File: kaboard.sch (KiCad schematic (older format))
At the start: 22 parts, among them IC1 ATMEGA8-P, K1 CONN_3, K2 CONN_3, K3 CONN_3, P1 CONN_6, P2 CONN_6, P3 CONN_6, P4 CONN_6, P5 CONN_5, P6 CONN_6, P7 CONN_5, P8 CONN_6, P9 CONN_5, SW1 SW_PUSH, X1 CRYSTAL

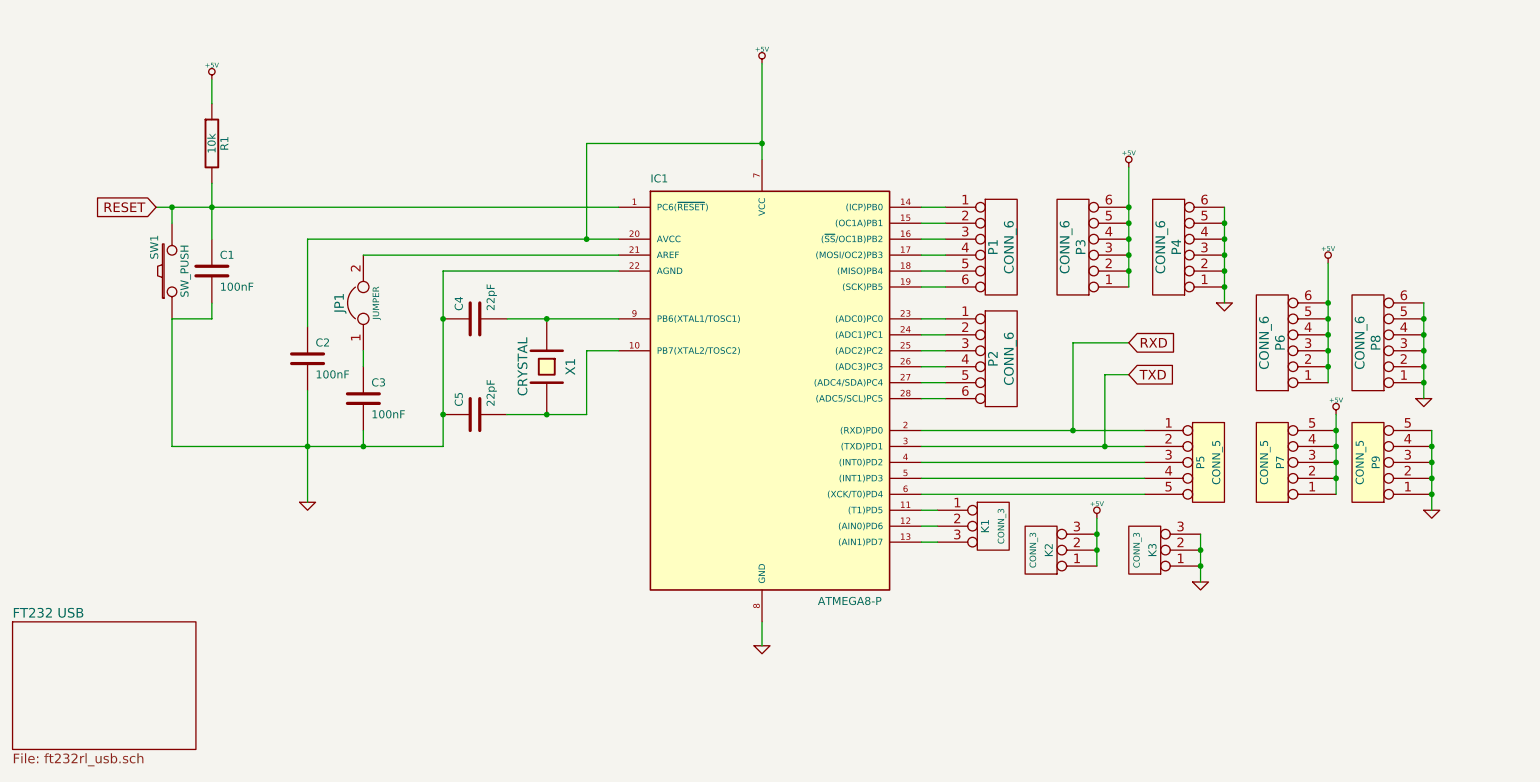
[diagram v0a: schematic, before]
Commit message: - Second version of the board - Added README for github
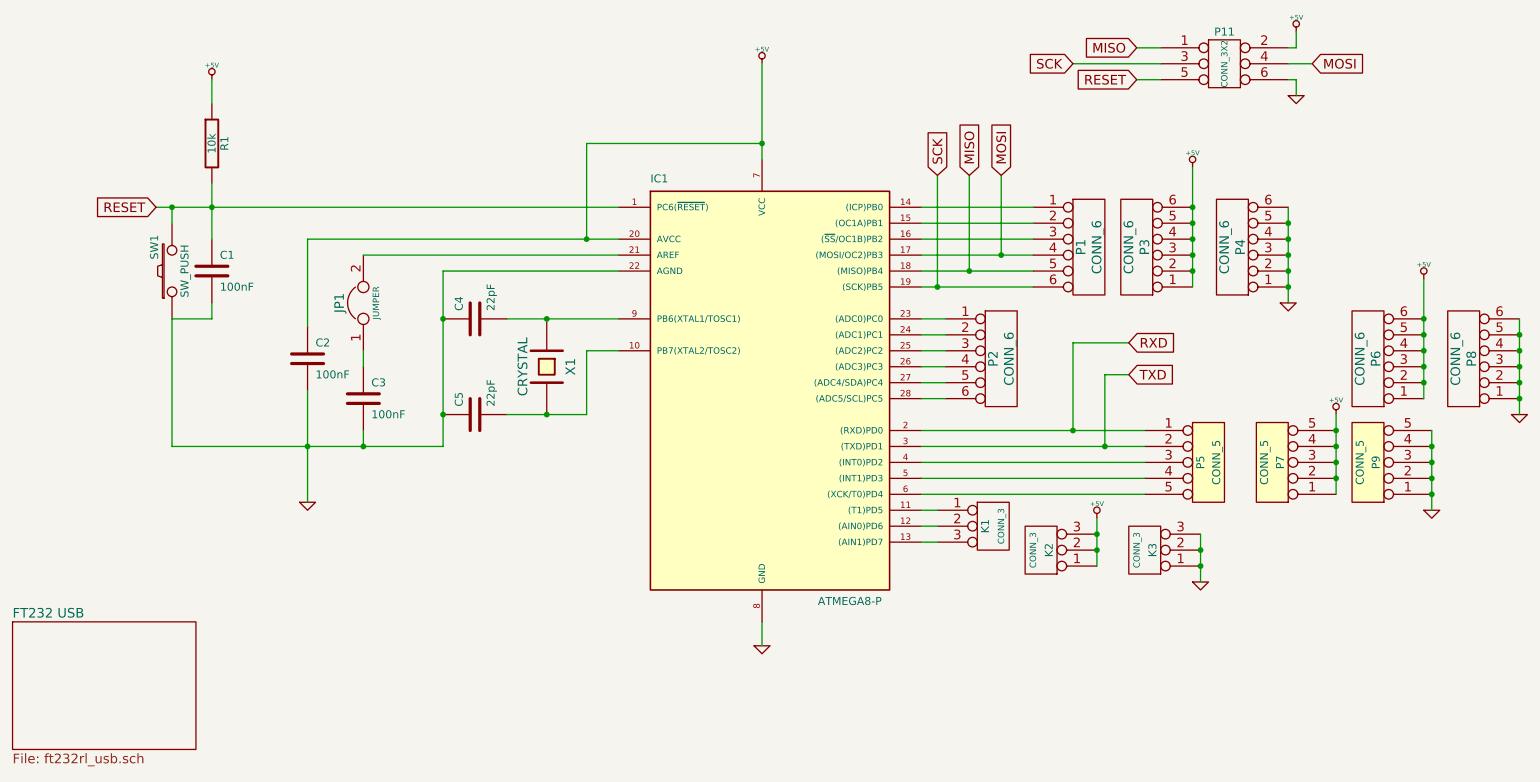
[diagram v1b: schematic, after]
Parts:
- added P11: CONN_3X2, symbol CONN_3X2
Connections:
- net +5V: now also P11.2
- net GND: now also P11.6
- net RESET: now also P11.5
- net MOSI: now reaches IC1.17 ((MOSI/OC2)PB3), P1.4
- net MOSI: now also P11.4
- net MISO: now reaches IC1.18 ((MISO)PB4), P1.5
- net MISO: now also P11.1
- net SCK: now reaches IC1.19 ((SCK)PB5), P1.6
- net SCK: now also P11.3
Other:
- moved on the sheet: P1, P3, P4, P6, P8
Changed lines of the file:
@@
-EESchema Schematic File Version 2  date Sun 09 Dec 2012 11:53:08 PM CET
+EESchema Schematic File Version 2  date Thu 13 Dec 2012 04:01:05 PM CET
 LIBS:power
 LIBS:device
@@
 Sheet 1 2
 Title ""
-Date "9 dec 2012"
+Date "13 dec 2012"
 Rev ""
 Comp ""
@@
 Connection ~ 9750 5450
 Wire Wire Line
-	9750 5550 9750 5050
+	9750 5050 9750 5550
 Connection ~ 9750 5250
 Connection ~ 9150 5250
 Connection ~ 9150 5050
-Connection ~ 9700 4350
+Connection ~ 10300 4450
+Connection ~ 10300 4650
 Connection ~ 9700 4550
-Connection ~ 9100 4450
-Connection ~ 9100 4650
-Connection ~ 9100 4550
-Connection ~ 9100 4350
+Connection ~ 9700 4750
 Connection ~ 9700 4650
 Connection ~ 9700 4450
-Wire Wire Line
-	9100 4000 9100 4750
-Connection ~ 9100 4250
-Wire Wire Line
-	9700 4850 9700 4250
-Connection ~ 9700 4750
-Connection ~ 8450 4150
-Wire Wire Line
-	8450 4250 8450 3650
-Connection ~ 7850 3650
-Wire Wire Line
-	7850 3400 7850 4150
-Connection ~ 8450 3850
-Connection ~ 8450 4050
-Connection ~ 7850 3750
-Connection ~ 7850 3950
+Connection ~ 10300 4750
+Connection ~ 10300 4550
+Wire Wire Line
+	9700 4100 9700 4850
+Connection ~ 9700 4350
+Wire Wire Line
+	10300 4350 10300 4950
+Connection ~ 10300 4850
+Connection ~ 8850 4150
+Wire Wire Line
+	8850 3650 8850 4250
+Connection ~ 8250 3650
+Wire Wire Line
+	8250 3400 8250 4150
+Connection ~ 8850 3850
+Connection ~ 8850 4050
+Connection ~ 8250 3750
+Connection ~ 8250 3950
 Wire Wire Line
 	6550 5350 7950 5350
@@
 	6550 5550 6650 5550
 Wire Wire Line
-	7950 5150 6550 5150
+	6550 5150 7950 5150
 Wire Wire Line
 	6550 4850 6700 4850
@@
 	6550 4450 6700 4450
 Wire Wire Line
-	6550 4150 6700 4150
-Wire Wire Line
-	6550 3950 6700 3950
-Wire Wire Line
-	6550 3750 6700 3750
+	6550 4150 7250 4150
+Wire Wire Line
+	6550 3950 7250 3950
+Wire Wire Line
+	6550 3750 7250 3750
 Wire Wire Line
 	5550 6400 5550 6250
@@
 Connection ~ 3550 4350
 Wire Wire Line
-	4650 3850 2700 3850
-Wire Wire Line
-	4650 4350 3950 4350
+	2700 3850 4650 3850
+Wire Wire Line
+	3950 4350 4650 4350
 Connection ~ 4200 4950
 Wire Wire Line
@@
 	4450 3250 5550 3250
 Wire Wire Line
-	2100 3850 2100 3500
+	2100 3500 2100 3850
 Wire Wire Line
 	5550 2750 5550 3350
@@
 Connection ~ 3050 5150
 Wire Wire Line
-	2700 5500 2700 4800
-Wire Wire Line
-	6550 3650 6700 3650
-Wire Wire Line
-	6550 3850 6700 3850
-Wire Wire Line
-	6550 4050 6700 4050
+	2700 4800 2700 5500
+Wire Wire Line
+	6550 3650 7250 3650
+Wire Wire Line
+	6550 3850 7250 3850
+Wire Wire Line
+	6550 4050 7250 4050
 Wire Wire Line
 	6700 4350 6550 4350
@@
 	6550 4750 6700 4750
 Wire Wire Line
-	7950 5050 6550 5050
+	6550 5050 7950 5050
 Wire Wire Line
 	7950 5250 6550 5250
@@
 Wire Wire Line
 	6550 5450 7950 5450
-Connection ~ 7850 4050
-Connection ~ 7850 3850
-Connection ~ 8450 3950
-Connection ~ 8450 3750
+Connection ~ 8250 4050
+Connection ~ 8250 3850
+Connection ~ 8850 3950
+Connection ~ 8850 3750
 Connection ~ 9150 5150
 Wire Wire Line
-	9150 5450 9150 4950
+	9150 4950 9150 5450
 Connection ~ 9150 5350
 Connection ~ 9750 5150
 Connection ~ 9750 5350
 Wire Wire Line
-	8300 6000 8300 5700
+	8300 5700 8300 6000
 Connection ~ 8300 5900
 Text GLabel 1750 3650 0    60   Input ~ 0
@@
 L CONN_6 P6
 U 1 1 5069D2A4
-P 8750 4500
-F 0 "P6" V 8700 4500 60  0000 C CNN
-F 1 "CONN_6" V 8800 4500 60  0000 C CNN
-	1    8750 4500
+P 9350 4600
+F 0 "P6" V 9300 4600 60  0000 C CNN
+F 1 "CONN_6" V 9400 4600 60  0000 C CNN
+	1    9350 4600
 	-1   0    0    1
 $EndComp
@@
 L CONN_6 P8
 U 1 1 5069D2A3
-P 9350 4500
-F 0 "P8" V 9300 4500 60  0000 C CNN
-F 1 "CONN_6" V 9400 4500 60  0000 C CNN
-	1    9350 4500
+P 9950 4600
+F 0 "P8" V 9900 4600 60  0000 C CNN
+F 1 "CONN_6" V 10000 4600 60  0000 C CNN
+	1    9950 4600
 	-1   0    0    1
 $EndComp
@@
 L GND #PWR06
 U 1 1 5069D2A2
-P 9700 4850
-F 0 "#PWR06" H 9700 4850 30  0001 C CNN
-F 1 "GND" H 9700 4780 30  0001 C CNN
-	1    9700 4850
+P 10300 4950
+F 0 "#PWR06" H 10300 4950 30  0001 C CNN
+F 1 "GND" H 10300 4880 30  0001 C CNN
+	1    10300 4950
 	1    0    0    -1
 $EndComp
@@
 L +5V #PWR07
 U 1 1 5069D2A1
-P 9100 4000
-F 0 "#PWR07" H 9100 4090 20  0001 C CNN
-F 1 "+5V" H 9100 4090 30  0000 C CNN
-	1    9100 4000
+P 9700 4100
+F 0 "#PWR07" H 9700 4190 20  0001 C CNN
+F 1 "+5V" H 9700 4190 30  0000 C CNN
+	1    9700 4100
 	1    0    0    -1
 $EndComp
@@
 L +5V #PWR08
 U 1 1 5069D26F
-P 7850 3400
-F 0 "#PWR08" H 7850 3490 20  0001 C CNN
-F 1 "+5V" H 7850 3490 30  0000 C CNN
-	1    7850 3400
+P 8250 3400
+F 0 "#PWR08" H 8250 3490 20  0001 C CNN
+F 1 "+5V" H 8250 3490 30  0000 C CNN
+	1    8250 3400
 	1    0    0    -1
 $EndComp
@@
 L GND #PWR09
 U 1 1 5069D267
-P 8450 4250
-F 0 "#PWR09" H 8450 4250 30  0001 C CNN
-F 1 "GND" H 8450 4180 30  0001 C CNN
-	1    8450 4250
+P 8850 4250
+F 0 "#PWR09" H 8850 4250 30  0001 C CNN
+F 1 "GND" H 8850 4180 30  0001 C CNN
+	1    8850 4250
 	1    0    0    -1
 $EndComp
@@
 L CONN_6 P4
 U 1 1 5069D139
-P 8100 3900
-F 0 "P4" V 8050 3900 60  0000 C CNN
-F 1 "CONN_6" V 8150 3900 60  0000 C CNN
-	1    8100 3900
+P 8500 3900
+F 0 "P4" V 8450 3900 60  0000 C CNN
+F 1 "CONN_6" V 8550 3900 60  0000 C CNN
+	1    8500 3900
 	-1   0    0    1
 $EndComp
@@
 L CONN_6 P3
 U 1 1 5069D130
-P 7500 3900
-F 0 "P3" V 7450 3900 60  0000 C CNN
-F 1 "CONN_6" V 7550 3900 60  0000 C CNN
-	1    7500 3900
+P 7900 3900
+F 0 "P3" V 7850 3900 60  0000 C CNN
+F 1 "CONN_6" V 7950 3900 60  0000 C CNN
+	1    7900 3900
 	-1   0    0    1
 $EndComp
@@
 L CONN_6 P1
 U 1 1 5069CE7E
-P 7050 3900
-F 0 "P1" V 7000 3900 60  0000 C CNN
-F 1 "CONN_6" V 7100 3900 60  0000 C CNN
-	1    7050 3900
+P 7600 3900
+F 0 "P1" V 7550 3900 60  0000 C CNN
+F 1 "CONN_6" V 7650 3900 60  0000 C CNN
+	1    7600 3900
 	1    0    0    -1
 $EndComp
@@
 F1 "ft232rl_usb.sch" 60
 $EndSheet
+$Comp
+L CONN_3X2 P11
+U 1 1 50C6F989
+P 8450 2800
+F 0 "P11" H 8450 3050 50  0000 C CNN
+F 1 "CONN_3X2" V 8450 2850 40  0000 C CNN
+	1    8450 2800
+	1    0    0    -1
+$EndComp
+$Comp
+L GND #PWR013
+U 1 1 50C6F9DA
+P 8900 2950
+F 0 "#PWR013" H 8900 2950 30  0001 C CNN
+F 1 "GND" H 8900 2880 30  0001 C CNN
+	1    8900 2950
+	1    0    0    -1
+$EndComp
+Wire Wire Line
+	8900 2950 8900 2850
+Wire Wire Line
+	8900 2850 8850 2850
+$Comp
+L +5V #PWR014
+U 1 1 50C6FA7D
+P 8900 2550
+F 0 "#PWR014" H 8900 2640 20  0001 C CNN
+F 1 "+5V" H 8900 2640 30  0000 C CNN
+	1    8900 2550
+	1    0    0    -1
+$EndComp
+Wire Wire Line
+	8850 2650 8900 2650
+Wire Wire Line
+	8900 2650 8900 2550
+Text GLabel 7900 2850 0    60   Input ~ 0
+RESET
+Wire Wire Line
+	7900 2850 8050 2850
+Text GLabel 7500 2750 0    60   Input ~ 0
+SCK
+Text GLabel 7900 2650 0    60   Input ~ 0
+MISO
+Wire Wire Line
+	7900 2650 8050 2650
+Wire Wire Line
+	7500 2750 8050 2750
+Text GLabel 9000 2750 2    60   Input ~ 0
+MOSI
+Wire Wire Line
+	8850 2750 9000 2750
+Text GLabel 6650 3450 1    60   Input ~ 0
+SCK
+Wire Wire Line
+	6650 4150 6650 3450
+Connection ~ 6650 4150
+Text GLabel 6850 3450 1    60   Input ~ 0
+MISO
+Wire Wire Line
+	6850 4050 6850 3450
+Connection ~ 6850 4050
+Text GLabel 7050 3450 1    60   Input ~ 0
+MOSI
+Wire Wire Line
+	7050 3950 7050 3450
+Connection ~ 7050 3950
 $EndSCHEMATC

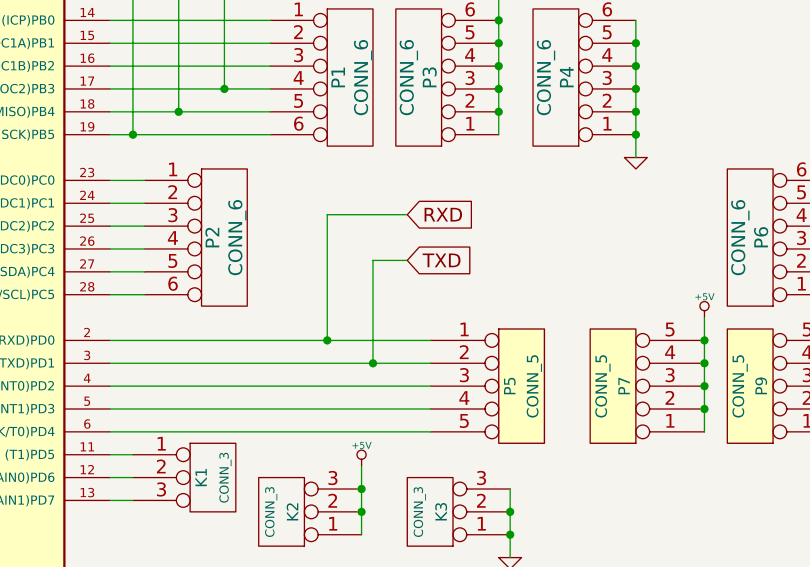
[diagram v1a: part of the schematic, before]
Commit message: Added list of known bugs on 1.0 Fixed the bugs and incremented version to 1.1
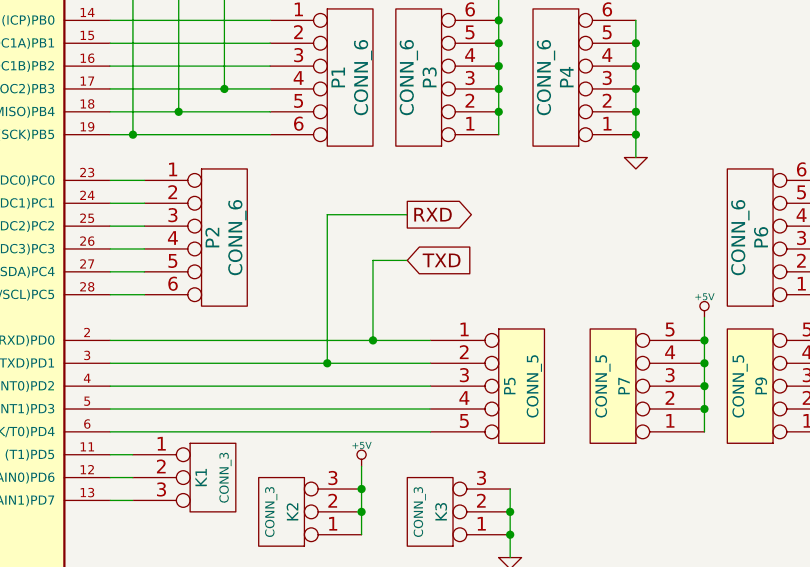
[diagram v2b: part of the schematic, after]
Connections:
- net RXD: now also IC1.3 ((TXD)PD1), P5.2; no longer IC1.2 ((RXD)PD0), P5.1
- net TXD: now also IC1.2 ((RXD)PD0), P5.1; no longer IC1.3 ((TXD)PD1), P5.2
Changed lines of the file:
@@
-EESchema Schematic File Version 2  date Thu 13 Dec 2012 04:01:05 PM CET
+EESchema Schematic File Version 2  date Thu 10 Jan 2013 10:06:40 AM CET
 LIBS:power
 LIBS:device
@@
 encoding utf-8
 Sheet 1 2
-Title ""
-Date "13 dec 2012"
-Rev ""
+Title "Kaboard"
+Date "10 jan 2013"
+Rev "1.1"
 Comp ""
 Comment1 ""
@@
 Wire Wire Line
 	7850 4700 7700 4700
-Connection ~ 7700 5150
-Wire Wire Line
-	7700 4700 7700 5150
 Wire Wire Line
 	6550 5750 6650 5750
@@
 Wire Wire Line
 	6550 5650 6650 5650
-Wire Wire Line
-	7500 5050 7500 4500
-Connection ~ 7500 5050
 Wire Wire Line
 	7500 4500 7850 4500
@@
 RESET
 $Comp
-L +5V #PWR01
+L +5V #PWR1
 U 1 1 5069D445
 P 2100 2850
-F 0 "#PWR01" H 2100 2940 20  0001 C CNN
+F 0 "#PWR1" H 2100 2940 20  0001 C CNN
 F 1 "+5V" H 2100 2940 30  0000 C CNN
 	1    2100 2850
@@
 $EndComp
 $Comp
-L +5V #PWR02
+L +5V #PWR5
 U 1 1 5069D42A
 P 7650 5600
-F 0 "#PWR02" H 7650 5690 20  0001 C CNN
+F 0 "#PWR5" H 7650 5690 20  0001 C CNN
 F 1 "+5V" H 7650 5690 30  0000 C CNN
 	1    7650 5600
@@
 $EndComp
 $Comp
-L GND #PWR03
+L GND #PWR7
 U 1 1 5069D427
 P 8300 6000
-F 0 "#PWR03" H 8300 6000 30  0001 C CNN
+F 0 "#PWR7" H 8300 6000 30  0001 C CNN
 F 1 "GND" H 8300 5930 30  0001 C CNN
 	1    8300 6000
@@
 $EndComp
 $Comp
-L GND #PWR04
+L GND #PWR13
 U 1 1 5069D3DB
 P 9750 5550
-F 0 "#PWR04" H 9750 5550 30  0001 C CNN
+F 0 "#PWR13" H 9750 5550 30  0001 C CNN
 F 1 "GND" H 9750 5480 30  0001 C CNN
 	1    9750 5550
@@
 $EndComp
 $Comp
-L +5V #PWR05
+L +5V #PWR11
 U 1 1 5069D354
 P 9150 4950
-F 0 "#PWR05" H 9150 5040 20  0001 C CNN
+F 0 "#PWR11" H 9150 5040 20  0001 C CNN
 F 1 "+5V" H 9150 5040 30  0000 C CNN
 	1    9150 4950
@@
 $EndComp
 $Comp
-L GND #PWR06
+L GND #PWR14
 U 1 1 5069D2A2
 P 10300 4950
-F 0 "#PWR06" H 10300 4950 30  0001 C CNN
+F 0 "#PWR14" H 10300 4950 30  0001 C CNN
 F 1 "GND" H 10300 4880 30  0001 C CNN
 	1    10300 4950
@@
 $EndComp
 $Comp
-L +5V #PWR07
+L +5V #PWR12
 U 1 1 5069D2A1
 P 9700 4100
-F 0 "#PWR07" H 9700 4190 20  0001 C CNN
+F 0 "#PWR12" H 9700 4190 20  0001 C CNN
 F 1 "+5V" H 9700 4190 30  0000 C CNN
 	1    9700 4100
@@
 $EndComp
 $Comp
-L +5V #PWR08
+L +5V #PWR6
 U 1 1 5069D26F
 P 8250 3400
-F 0 "#PWR08" H 8250 3490 20  0001 C CNN
+F 0 "#PWR6" H 8250 3490 20  0001 C CNN
 F 1 "+5V" H 8250 3490 30  0000 C CNN
 	1    8250 3400
@@
 $EndComp
 $Comp
-L GND #PWR09
+L GND #PWR8
 U 1 1 5069D267
 P 8850 4250
-F 0 "#PWR09" H 8850 4250 30  0001 C CNN
+F 0 "#PWR8" H 8850 4250 30  0001 C CNN
 F 1 "GND" H 8850 4180 30  0001 C CNN
 	1    8850 4250
@@
 	-1   0    0    1
 $EndComp
-Text GLabel 7850 4500 2    60   Input ~ 0
+Text GLabel 7850 4500 2    60   Output ~ 0
 RXD
 Text GLabel 7850 4700 2    60   Input ~ 0
@@
 $EndComp
 $Comp
-L GND #PWR010
+L GND #PWR4
 U 1 1 5069BC71
 P 5550 6400
-F 0 "#PWR010" H 5550 6400 30  0001 C CNN
+F 0 "#PWR4" H 5550 6400 30  0001 C CNN
 F 1 "GND" H 5550 6330 30  0001 C CNN
 	1    5550 6400
@@
 $EndComp
 $Comp
-L +5V #PWR011
+L +5V #PWR3
 U 1 1 5069BBAF
 P 5550 2750
-F 0 "#PWR011" H 5550 2840 20  0001 C CNN
+F 0 "#PWR3" H 5550 2840 20  0001 C CNN
 F 1 "+5V" H 5550 2840 30  0000 C CNN
 	1    5550 2750
@@
 $EndComp
 $Comp
-L GND #PWR012
+L GND #PWR2
 U 1 1 5069B4FE
 P 2700 5500
-F 0 "#PWR012" H 2700 5500 30  0001 C CNN
+F 0 "#PWR2" H 2700 5500 30  0001 C CNN
 F 1 "GND" H 2700 5430 30  0001 C CNN
 	1    2700 5500
@@
 $EndComp
 $Comp
-L GND #PWR013
+L GND #PWR10
 U 1 1 50C6F9DA
 P 8900 2950
-F 0 "#PWR013" H 8900 2950 30  0001 C CNN
+F 0 "#PWR10" H 8900 2950 30  0001 C CNN
 F 1 "GND" H 8900 2880 30  0001 C CNN
 	1    8900 2950
@@
 	8900 2850 8850 2850
 $Comp
-L +5V #PWR014
+L +5V #PWR9
 U 1 1 50C6FA7D
 P 8900 2550
-F 0 "#PWR014" H 8900 2640 20  0001 C CNN
+F 0 "#PWR9" H 8900 2640 20  0001 C CNN
 F 1 "+5V" H 8900 2640 30  0000 C CNN
 	1    8900 2550
@@
 	7050 3950 7050 3450
 Connection ~ 7050 3950
+Wire Wire Line
+	7500 5150 7500 4500
+Connection ~ 7500 5150
+Wire Wire Line
+	7700 4700 7700 5050
+Connection ~ 7700 5050
 $EndSCHEMATC

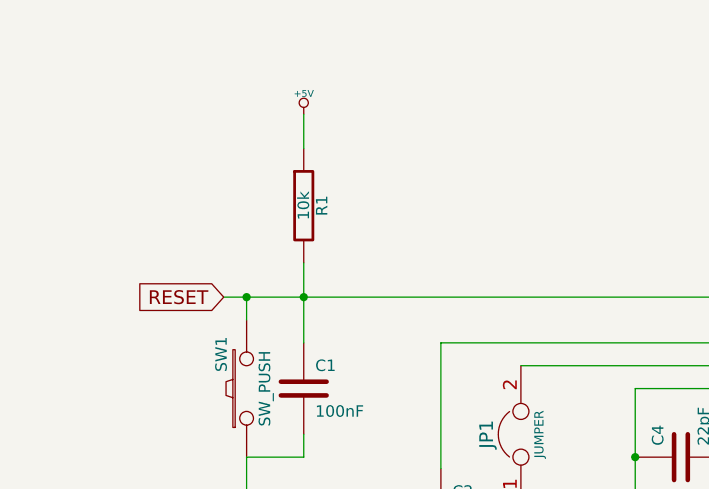
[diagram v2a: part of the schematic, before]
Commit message: Small fixed to make the reset circut more reliable
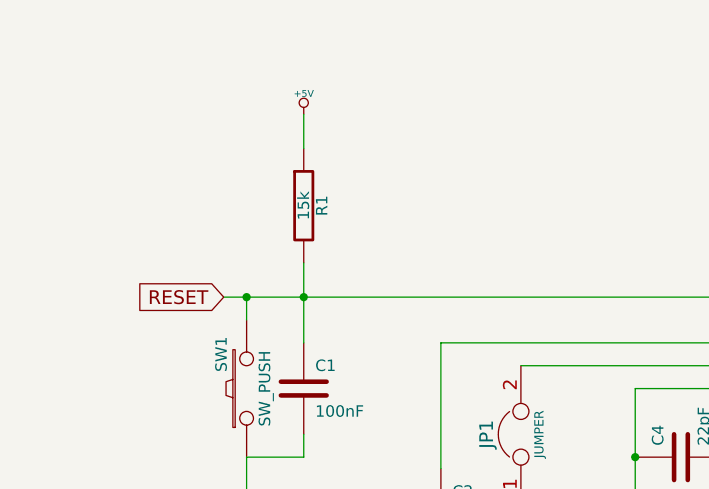
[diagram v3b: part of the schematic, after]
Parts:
- R1: value 10k -> 15k
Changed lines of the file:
@@
-EESchema Schematic File Version 2  date Thu 10 Jan 2013 10:06:40 AM CET
+EESchema Schematic File Version 2  date Thu 17 Jan 2013 01:01:30 PM CET
 LIBS:power
 LIBS:device
@@
 Sheet 1 2
 Title "Kaboard"
-Date "10 jan 2013"
+Date "17 jan 2013"
 Rev "1.1"
 Comp ""
@@
 P 2100 3250
 F 0 "R1" V 2180 3250 50  0000 C CNN
-F 1 "10k" V 2100 3250 50  0000 C CNN
+F 1 "15k" V 2100 3250 50  0000 C CNN
 	1    2100 3250
 	1    0    0    -1
